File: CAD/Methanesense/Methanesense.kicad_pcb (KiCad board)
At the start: 4 copper layers, 31.4 x 21 mm, 69 parts, among them J1 Conn_01x06_Pin, J2 SM12B-GHS-TB(LF)(SN), U1 AP63201WU, U2 ADS1115IDGS, U3 ESP32-C3-WROOM-02, U4 LP5907MFX-3.0, U5 MCP4725xxx-xCH, Y1 32.768khz 3215 12.5pf

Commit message: WIP
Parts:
- removed D1, D2, D3, D4: 1N5819WS, Diode_SMD:D_SOD-323
- removed R14: 182k, Resistor_SMD:R_0402_1005Metric
- removed R15: 62k, Resistor_SMD:R_0402_1005Metric
- removed R16: 10K, Resistor_SMD:R_0402_1005Metric
- removed U1: AP63201WU, Package_TO_SOT_SMD:TSOT-23-6
- removed Y1: 32.768khz 3215 12.5pf, Crystal:Crystal_SMD_3215-2Pin_3.2x1.5mm
- removed kibuzzard-65D3616E: G***, esprelay:kibuzzard-65D3616E
- removed kibuzzard-65D36177: G***, esprelay:kibuzzard-65D36177
- removed kibuzzard-65D46022: G***, esprelay:kibuzzard-65D46022
- removed kibuzzard-65D46066: G***, esprelay:kibuzzard-65D46066
- removed kibuzzard-65D460A0: G***, esprelay:kibuzzard-65D460A0
- removed kibuzzard-65D49092: G***, kibuzzard-65D49092
- removed kibuzzard-65D7176D: G***, kibuzzard-65D7176D
- removed kibuzzard-65D71774: G***, kibuzzard-65D71774
- removed kibuzzard-65D7177B: G***, kibuzzard-65D7177B
- removed kibuzzard-65D74DE1: G***, kibuzzard-65D74DE1
- removed kibuzzard-65D74DEE: G***, kibuzzard-65D74DEE
- removed kibuzzard-65D74DFB: G***, kibuzzard-65D74DFB
- removed kibuzzard-65D8B121: G***, kibuzzard-65D8B121
- removed kibuzzard-65DC95DA: G***, kibuzzard-65DC95DA
- removed kibuzzard-65DC95E5: G***, kibuzzard-65DC95E5
- removed kibuzzard-65DC95EF: G***, kibuzzard-65DC95EF
- removed kibuzzard-65DC95F6: G***, kibuzzard-65DC95F6
- removed kibuzzard-65DC9610: G***, kibuzzard-65DC9610
- removed kibuzzard-65DC961D: G***, kibuzzard-65DC961D
- removed kibuzzard-65DCE4DE: G***, kibuzzard-65DCE4DE
- added BT1: 1042P, Battery:BatteryHolder_MPD_BH-18650-PC2, B.Cu at (64.8, 63.2)
- added C21: 47uF, Capacitor_SMD:C_0805_2012Metric, F.Cu at (44.8, 53.8)
- added C22: 47uF, Capacitor_SMD:C_0805_2012Metric, F.Cu at (63.8, 53.9)
- added C23: 4.7uF, Capacitor_SMD:C_0603_1608Metric, F.Cu at (57.2, 51.0)
- added C24: 1nF, Capacitor_SMD:C_0603_1608Metric, F.Cu at (62.4, 68.0)
- added C25: 4.7uF, Capacitor_SMD:C_0603_1608Metric, F.Cu at (51.2, 51.0)
- added C26: 15pF, Methanesense:C_0603_1608Metric, F.Cu at (54.6, 69.1)
- added C27: 15pF, Methanesense:C_0603_1608Metric, F.Cu at (54.4, 70.9)
- added C28: 1uF, Capacitor_SMD:C_0603_1608Metric, F.Cu at (68.7, 69.0)
- added C29: 56pF, Capacitor_SMD:C_0603_1608Metric, F.Cu at (62.2, 71.4)
- added C30: 56pF, Capacitor_SMD:C_0603_1608Metric, F.Cu at (60.2, 72.1)
- added C31: 1uF, Capacitor_SMD:C_0603_1608Metric, F.Cu at (66.6, 53.8)
- added C32: 0.1uF, Capacitor_SMD:C_0603_1608Metric, F.Cu at (47.6, 53.6)
- added C33: 15pF, Capacitor_SMD:C_0603_1608Metric, F.Cu at (46.3, 53.6)
- added C34: 0.1uF, Capacitor_SMD:C_0603_1608Metric, F.Cu at (62.2, 53.7)
- added C35: 15pF, Capacitor_SMD:C_0603_1608Metric, F.Cu at (60.8, 53.7)
- added C36: 0.1uF, Capacitor_SMD:C_0603_1608Metric, F.Cu at (54.4, 51.0)
- added C37: 10uF, Capacitor_SMD:C_0805_2012Metric, F.Cu at (88.6, 62.8)
- added C38: 0.1uF, Capacitor_SMD:C_0603_1608Metric, F.Cu at (139.0, 52.4)
- added C39: 1uF, Capacitor_SMD:C_0603_1608Metric, F.Cu at (137.5, 52.4)
- added D10: LED, LED_SMD:LED_0603_1608Metric, F.Cu at (80.7, 87.8)
- added D11: LED, LED_SMD:LED_0603_1608Metric, F.Cu at (80.7, 90.4)
- added D5: LED, LED_SMD:LED_0603_1608Metric, F.Cu at (95.6, 53.6)
- added D6: LED, LED_SMD:LED_0603_1608Metric, F.Cu at (98.6, 53.6)
- added D9: LED, LED_SMD:LED_0603_1608Metric, F.Cu at (80.7, 85.2)
- added F1: 0805L110WR, Resistor_SMD:R_1206_3216Metric, F.Cu at (68.8, 63.4)
- added J3: 693043020611, Methanesense:693043020611, F.Cu at (74.8, 55.5)
- added J4: Conn_Coaxial, Connector_Coaxial:U.FL_Hirose_U.FL-R-SMT-1_Vertical, F.Cu at (66.2, 72.2)
- added J6: JLINK, esprelay:SEXY_pinpogo, B.Cu at (47.0, 61.0)
- added J7: Conn_02x05_Odd_Even, Connector_PinHeader_2.54mm:PinHeader_2x05_P2.54mm_Vertical, F.Cu at (74.8, 42.8)
- added L2: 39NH, Methanesense:L_0603_1608Metric, F.Cu at (56.4, 72.0)
- added L3: 2.2uH, Inductor_SMD:L_1008_2520Metric, F.Cu at (86.2, 70.2)
- added L4: NP, Methanesense:L_0603_1608Metric, F.Cu at (49.8, 73.9)
- added L5: 7.5NH, Methanesense:L_0603_1608Metric, F.Cu at (46.0, 73.9)
- added L6: 1.6nH, Methanesense:L_0603_1608Metric, F.Cu at (44.1, 74.5)
- added L7: 39NH, Methanesense:L_0603_1608Metric, F.Cu at (51.8, 70.7)
- added L8: 68 nH, Methanesense:L_0603_1608Metric, F.Cu at (63.6, 71.5)
- added NT1: NetTie_2, esprelay:Viatie, F.Cu at (89.7, 68.0)
- added Q1: FDS6892A, Package_SO:SOIC-8_3.9x4.9mm_P1.27mm, F.Cu at (128.8, 70.1)
- added Q2: FDS6892A, Package_SO:SOIC-8_3.9x4.9mm_P1.27mm, F.Cu at (97.2, 58.2)
- added R17: 1M, Resistor_SMD:R_0603_1608Metric, F.Cu at (68.7, 67.1)
- added R18: 100R, Capacitor_SMD:C_0603_1608Metric, F.Cu at (65.9, 56.6)
- added R19: 100R, Capacitor_SMD:C_0603_1608Metric, F.Cu at (65.9, 58.1)
- added R20: 100R, Capacitor_SMD:C_0603_1608Metric, F.Cu at (65.9, 59.6)
- added R22: 120R, Capacitor_SMD:C_0603_1608Metric, F.Cu at (98.6, 52.0)
- added R23: 120R, Capacitor_SMD:C_0603_1608Metric, F.Cu at (95.6, 52.0)
- added R24: 1M, Resistor_SMD:R_0603_1608Metric, F.Cu at (98.8, 62.6)
- added R25: 1M, Resistor_SMD:R_0603_1608Metric, F.Cu at (95.8, 62.6)
- added R26: 1k, Capacitor_SMD:C_0603_1608Metric, F.Cu at (168.8, 96.2)
- added S1: TGS8410, Methanesense:TGS8410, B.Cu at (145.9, 70.8)
- added SW1: KMR223GLFG, Button_Switch_SMD:SW_Push_1P1T_NO_CK_KMR2, F.Cu at (171.1, 82.4)
- added SW2: JS202011JCQN, Button_Switch_SMD:SW_DIP_SPSTx01_Slide_6.7x4.1mm_W6.73mm_P2.54mm_LowProfile_JPin, F.Cu at (165.9, 92.7)
- added SW3: KMR223GLFG, Button_Switch_SMD:SW_Push_1P1T_NO_CK_KMR2, F.Cu at (77.5, 81.6)
- added TH1: 10k NTC, Resistor_SMD:R_0603_1608Metric, F.Cu at (84.0, 90.9)
- added U6: BME680, Package_LGA:Bosch_LGA-8_3x3mm_P0.8mm_ClockwisePinNumbering, F.Cu at (148.4, 52.0)
- added U7: FT230XQ, Package_DFN_QFN:QFN-16-1EP_4x4mm_P0.65mm_EP2.1x2.1mm, F.Cu at (127.4, 56.8)
- added U8: USBLC6-4SC6, Package_TO_SOT_SMD:SOT-23-6, F.Cu at (62.1, 58.3)
- added U9: TPS22917DBV, Package_TO_SOT_SMD:SOT-23-6, F.Cu at (65.2, 68.0)
- C1: value 20pf -> 1.7pF; footprint Capacitor_SMD:C_0402_1005Metric -> Methanesense:C_0603_1608Metric
- C10: value 0.1uF -> 10uF; footprint Capacitor_SMD:C_0402_1005Metric -> Capacitor_SMD:C_0805_2012Metric
- C11, C8: value 22uf -> 1uF; footprint Capacitor_SMD:C_0402_1005Metric -> Capacitor_SMD:C_0603_1608Metric
- C12: value 22uf -> 10uF; footprint Capacitor_SMD:C_0402_1005Metric -> Capacitor_SMD:C_0805_2012Metric
- C13, C14, C15, C16, C20: footprint Capacitor_SMD:C_0402_1005Metric -> Capacitor_SMD:C_0603_1608Metric
- C17, C18, C9: value 0.1uF -> 1uF; footprint Capacitor_SMD:C_0402_1005Metric -> Capacitor_SMD:C_0603_1608Metric
- C19: value 1uF -> 0.1uF; footprint Capacitor_SMD:C_0402_1005Metric -> Capacitor_SMD:C_0603_1608Metric
- C2: value 0.1uF -> 1.7pF; footprint Capacitor_SMD:C_0402_1005Metric -> Methanesense:C_0603_1608Metric
- C3, C6: value 0.1uF -> 47pF; footprint Capacitor_SMD:C_0402_1005Metric -> Capacitor_SMD:C_0603_1608Metric
- C4: value 20pf -> 8.5pF; footprint Capacitor_SMD:C_0402_1005Metric -> Methanesense:C_0603_1608Metric
- C5: value 10uF -> 15pF; footprint Capacitor_SMD:C_0805_2012Metric -> Methanesense:C_0603_1608Metric
- C7: value 10uF -> 1uF; footprint Capacitor_SMD:C_0805_2012Metric -> Capacitor_SMD:C_0603_1608Metric
- J1: value Conn_01x06_Pin -> USB_C_Receptacle_USB2.0_14P; footprint TestPoint:TestPoint_Pad_1.0x1.0mm_6pad -> Methanesense:USB_C_Receptacle_HCTL_HC-TYPE-C-16P-01A; moved to F.Cu
- J2: value SM12B-GHS-TB(LF)(SN) -> Conn_Coaxial; footprint Connector_JST:JST_GH_SM12B-GHS-TB_1x12-1MP_P1.25mm_Horizontal -> Connector_Coaxial:U.FL_Hirose_U.FL-R-SMT-1_Vertical
- L1: value 6.8uH -> 2.3nH; footprint Inductor_SMD:L_1008_2520Metric -> Methanesense:L_0603_1608Metric
- R1: value 10K -> 68k; footprint Resistor_SMD:R_0402_1005Metric -> Resistor_SMD:R_0603_1608Metric
- R10, R11: value 499R -> 1M; footprint Resistor_SMD:R_0402_1005Metric -> Resistor_SMD:R_0603_1608Metric
- R12: value 10K -> 10k; footprint Resistor_SMD:R_0402_1005Metric -> Resistor_SMD:R_0603_1608Metric
- R13: value 100R -> 10k; footprint Resistor_SMD:R_0402_1005Metric -> Resistor_SMD:R_0603_1608Metric
- R2, R3, R4, R5: value 10K -> 499R
- R6: footprint Resistor_SMD:R_0402_1005Metric -> Resistor_SMD:R_0603_1608Metric
- R7: value 309k -> 499R
- R9: value 499R -> <2k; footprint Resistor_SMD:R_0402_1005Metric -> Resistor_SMD:R_0603_1608Metric
- U3: value ESP32-C3-WROOM-02 -> nPM1300-QEXX; footprint PCM_Espressif:ESP32-C3-WROOM-02 -> Package_DFN_QFN:QFN-32-1EP_5x5mm_P0.5mm_EP3.6x3.6mm; moved to F.Cu
- U4: value LP5907MFX-3.0 -> AP7331-20WG-7
- U5: value MCP4725xxx-xCH -> nRF9160-SICA; footprint Package_TO_SOT_SMD:SOT-23-6 -> PCM_nordic-lib-kicad-nrf9:LGA_9160_16.0x10.5mm
- moved J2 81.1 mm to (48.4, 71.3), turned to 180 degrees
- moved U5 69.0 mm to (54.5, 60.0)
- moved C2 68.7 mm to (51.0, 73.9), turned to 90 degrees
- moved C5 67.7 mm to (53.5, 70.9), turned to -135 degrees
- moved L1 64.3 mm to (52.9, 74.5), turned to 180 degrees
- moved C4 63.2 mm to (47.8, 74.5), turned to 180 degrees
- moved C7 54.3 mm to (136.3, 35.9), turned to 0 degrees
- moved C1 54.1 mm to (55.3, 74.5), turned to 180 degrees
- moved U4 53.8 mm to (136.4, 33.3), turned to 180 degrees
- moved C9 49.9 mm to (136.4, 30.9), turned to 0 degrees
- moved C6 47.2 mm to (132.1, 39.6), turned to 0 degrees
- moved C8 44.5 mm to (139.2, 33.3), turned to 90 degrees
- moved C3 44.2 mm to (132.1, 37.1), turned to 0 degrees
- moved R12 38.7 mm to (134.5, 52.4), turned to 90 degrees
- moved R13 38.4 mm to (136.0, 52.4), turned to 90 degrees
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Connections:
- C1 pad 1: GND -> Net-(C1-Pad1)
- C1 pad 2: Net-(U3-GPIO0/ADC1_CH0/XTAL_32K_P) -> Net-(C1-Pad2)
- C10 pad 1: +3.3V -> +2V0
- C10 pad 2: GND -> PVSS1
- C11 pad 1: +3.3V -> +5V
- C12 pad 1: +3.3V -> VSYS
- C13 pad 1: +3V0 -> GND
- C13 pad 2: GND -> Net-(U2-AIN0)
- C14 pad 1: +3.3V -> GND
- C14 pad 2: GND -> Net-(U2-AIN1)
- C15 pad 2: Net-(U2-AIN0) -> Net-(U2-AIN2)
- C16 pad 2: Net-(U2-AIN1) -> Net-(U2-AIN3)
- C17 pad 1: GND -> Net-(U2-AIN0)
- C17 pad 2: Net-(U2-AIN2) -> Net-(U2-AIN1)
- C18 pad 1: GND -> Net-(U2-AIN2)
- C19 pad 1: Net-(U2-AIN0) -> +2V0
- C19 pad 2: Net-(U2-AIN1) -> GND
- C2 pad 1: /SW -> Net-(C2-Pad1)
- C2 pad 2: Net-(U1-BST) -> GND
- C20 pad 1: Net-(U2-AIN2) -> +2V0
- C20 pad 2: Net-(U2-AIN3) -> GND
- C3 pad 1: +3.3V -> GND
- C3 pad 2: GND -> Net-(U7-USBDM)
- C4 pad 1: Net-(U3-GPIO1/ADC1_CH1/XTAL_32K_N) -> Net-(C2-Pad1)
- C4 pad 2: GND -> Net-(C4-Pad2)
- C5 pad 1: /VIN_P -> /nrf9160/ANT
- C5 pad 2: GND -> Net-(J2-In)
- C6 pad 1: +3V0 -> GND
- C6 pad 2: GND -> Net-(U7-USBDP)
- C7 pad 1: +3V0 -> Net-(U4-OUT)
- C8 pad 1: +3.3V -> +5VL
- C9 pad 1: +3.3V -> Net-(U4-BP)
- C9 pad 2: /FB -> GND
- J2 pad 1: +3.3V -> Net-(J2-In)
- J2 pad 2: ONEWIRE_OUT -> GND
- L1 pad 1: /SW -> Net-(C1-Pad2)
- L1 pad 2: +3.3V -> Net-(C2-Pad1)
- R1 pad 1: +3.3V -> Net-(U3-VSET1)
- R1 pad 2: RST -> GND
- R10 pad 1: Net-(U2-AIN2) -> GND
- R10 pad 2: AIN2 -> /Sensor
- R11 pad 1: Net-(U2-AIN3) -> GND
- R11 pad 2: AIN3 -> /Heater
- R12 pad 1: ADC_DRDY -> /nrf9160/SDA
- R12 pad 2: +3.3V -> +2V0
- R13 pad 1: ONEWIRE_OUT -> /nrf9160/SCL
- R13 pad 2: ONEWIRE -> +2V0
- R2 pad 1: +3.3V -> Net-(U2-AIN0)
- R2 pad 2: BOOT -> AIN0
- R3 pad 1: ADC -> Net-(U2-AIN1)
- R3 pad 2: GND -> AIN1
- R4 pad 1: Net-(U3-GPIO8) -> Net-(U2-AIN2)
- R4 pad 2: +3.3V -> AIN2
- R5 pad 1: SDA -> Net-(U2-AIN3)
- R5 pad 2: +3.3V -> AIN3
- R6 pad 1: +3.3V -> /ADC_DRDY
- R6 pad 2: ONEWIRE -> +2V0
- R7 pad 1: /VIN_P -> AIN0
- R7 pad 2: ADC -> AIN0
- R8 pad 1: Net-(U2-AIN0) -> AIN1
- R8 pad 2: AIN0 -> AIN1
- R9 pad 1: Net-(U2-AIN1) -> AIN1
- R9 pad 2: AIN1 -> AIN0
- U2 pad 10: SCL -> /SCL
- U2 pad 2: ADC_DRDY -> /ADC_DRDY
- U2 pad 8: +3V0 -> +2V0
- U2 pad 9: SDA -> /SDA
- U3 pad 1: +3.3V -> +2V0
- U3 pad 10: ADC_DRDY -> unconnected-(U3-GPIO3-Pad10)
- U3 pad 11: RX -> unconnected-(U3-GPIO4-Pad11)
- U3 pad 12: TX -> +2V0
- U3 pad 13: unconnected-(U3-GPIO18/USB_D--Pad13) -> /SDA
- U3 pad 14: SCL -> /SCL
- U3 pad 15: ONEWIRE -> Net-(U3-SHPHLD)
- U3 pad 16: SDA -> GND
- U3 pad 17: Net-(U3-GPIO1/ADC1_CH1/XTAL_32K_N) -> Net-(U3-VSET1)
- U3 pad 18: Net-(U3-GPIO0/ADC1_CH0/XTAL_32K_P) -> Net-(U3-NTC)
- U3 pad 19: GND -> +BATT
- U3 pad 2: RST -> PVSS1
- U3 pad 3: ADC -> /POWER/SW1
- U3 pad 4: unconnected-(U3-GPIO5/ADC2_CH0-Pad4) -> VSYS
- U3 pad 6: unconnected-(U3-GPIO7-Pad6) -> GND
- U3 pad 7: Net-(U3-GPIO8) -> unconnected-(U3-GPIO0-Pad7)
- U3 pad 8: BOOT -> unconnected-(U3-GPIO1-Pad8)
- U3 pad 9: GND -> unconnected-(U3-GPIO2-Pad9)
- U4 pad 1: +3.3V -> +5VL
- U4 pad 3: ENBL_PSUP -> +5VL
- U4 pad 4: unconnected-(U4-NC-Pad4) -> Net-(U4-BP)
- U4 pad 5: +3V0 -> Net-(U4-OUT)
- U5 pad 1: AOUT0 -> GND
- U5 pad 2: GND -> /nrf9160/P0.05
- U5 pad 3: +3.3V -> /nrf9160/P0.06
- U5 pad 4: SDA -> /nrf9160/P0.07
- U5 pad 5: SCL -> GND
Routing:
- net +3.3V: track 105.2 -> 0.00 mm, vias 10 -> 0
- net GND: track 42.8 -> 128.4 mm, vias 72 -> 65
- net +1V8SIM: track 0.00 -> 38.6 mm, vias 0 -> 2
- net +3V0: track 32.5 -> 0.00 mm, vias 2 -> 0
- net /nrf9160/SIM_CLK: track 0.00 -> 28.7 mm, vias 0 -> 2
- net /nrf9160/SIM_RST: track 0.00 -> 28.5 mm, vias 0 -> 2
- net /nrf9160/SIM_IO: track 0.00 -> 27.5 mm, vias 0 -> 2
- net SDA: track 27.2 -> 0.00 mm, vias 2 -> 0
- net SCL: track 25.6 -> 0.00 mm, vias 2 -> 0
- net RST: track 21.3 -> 0.00 mm, vias 2 -> 0
- net ONEWIRE: track 19.0 -> 0.00 mm, vias 1 -> 0
- net ADC_DRDY: track 17.9 -> 0.00 mm, vias 1 -> 0
- net BOOT: track 17.7 -> 0.00 mm, vias 1 -> 0
- net /nrf9160/COEX0: track 0.00 -> 16.2 mm
- net /VIN_P: track 16.2 -> 0.00 mm, vias 2 -> 0
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- removed copper zone on B.Cu, net +3.3V
- removed copper zone on F.Cu, net +3.3V
- removed copper zone on In1.Cu, net +3.3V
- removed copper zone on F.Cu, net +VDC
- removed copper zone on F.Cu, net /VIN_P
- removed copper zone on B.Cu, net GND
- removed copper zone on F.Cu, net GND
- removed copper zone on In1.Cu, net GND
- removed copper zone on In2.Cu, net GND
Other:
- board size 31.4 x 21 mm -> 120 x 25 mm
- board text removed: "1"
- board text removed: "2"
- board text removed: "3"
- board text removed: "4"

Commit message: WIP
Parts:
- removed NT1: NetTie_2, esprelay:Viatie
- BT1: moved to F.Cu
- moved TH1 31.2 mm to (70.9, 62.6)
- moved R1 27.0 mm to (73.6, 63.0), turned to 90 degrees
- moved SW3 19.0 mm to (77.2, 62.6), turned to 180 degrees
- moved D11 18.2 mm to (77.5, 72.5), turned to -90 degrees
- moved D10 16.0 mm to (76.0, 72.5), turned to -90 degrees
- moved C11 15.6 mm to (72.5, 68.5), turned to 180 degrees
- moved D9 14.1 mm to (74.5, 72.5), turned to -90 degrees
- moved C10 6.90 mm to (81.7, 70.2)
- moved C37 5.30 mm to (84.1, 65.6), turned to 90 degrees
- moved C12 4.45 mm to (82.1, 65.6), turned to 90 degrees
- moved U3 4.16 mm to (77.5, 67.5)
- moved C21 3.15 mm to (46.6, 51.2), turned to 180 degrees
- moved L3 2.06 mm to (84.2, 69.7)
- moved C29 1.38 mm to (61.4, 70.3), turned to 180 degrees
- moved F1 0.20 mm to (69.0, 63.4)
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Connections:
- C10 pad 2: PVSS1 -> GND
- U3 pad 2: PVSS1 -> GND
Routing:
- net +5VL: track 0.00 -> 50.7 mm, vias 0 -> 3
- net GND: track 128.4 -> 165.4 mm, vias 65 -> 79
- net +5V: track 11.3 -> 36.8 mm, vias 0 -> 3
- net +2V0: track 2.88 -> 16.0 mm
- net VSYS: track 0.00 -> 13.0 mm, vias 0 -> 4
- net +BATT: track 0.00 -> 6.83 mm
- net Net-(BT1-+): track 0.00 -> 4.66 mm
- net /POWER/SW1: track 0.00 -> 4.41 mm
- net /POWER/CC1: track 0.00 -> 2.78 mm, vias 0 -> 1
- net Net-(D9-K): track 0.00 -> 2.28 mm
- net /nrf9160/SIM_IO: track 27.5 -> 29.8 mm
- net Net-(D11-K): track 0.00 -> 2.07 mm
- net Net-(U3-SHPHLD): track 0.00 -> 2.00 mm
- net Net-(D10-K): track 0.00 -> 1.87 mm
- net Net-(U9-VOUT): track 2.09 -> 3.54 mm
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- added copper zone on F.Cu, net +2V0
- added copper zone on F.Cu, net +5V
- added copper zone on F.Cu, net /POWER/SW1
- added copper zone on F.Cu, net GND
- added copper zone on F.Cu, net VSYS

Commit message: Allmost there
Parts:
- removed C15, C16: 0.1uF, Capacitor_SMD:C_0603_1608Metric
- removed C18: 1uF, Capacitor_SMD:C_0603_1608Metric
- removed J7: Conn_02x05_Odd_Even, Connector_PinHeader_2.54mm:PinHeader_2x05_P2.54mm_Vertical
- removed R12, R13: 10k, Resistor_SMD:R_0603_1608Metric
- removed R6: 10K, Resistor_SMD:R_0603_1608Metric
- added AE1: NN02-220, Methanesense:XCVR_NN02-220, F.Cu at (37.0, 63.0)
- BT1: value 1042P -> BH-18650-PC2; footprint Battery:BatteryHolder_MPD_BH-18650-PC2 -> Methanesense:BatteryHolder_MPD_BH-18650-PC2; moved to B.Cu
- R2, R3: footprint Resistor_SMD:R_0402_1005Metric -> Resistor_SMD:R_0603_1608Metric
- R4, R5, R7, R8: value 499R -> 0R; footprint Resistor_SMD:R_0402_1005Metric -> Resistor_SMD:R_0603_1608Metric
- moved SW1 84.4 mm to (89.0, 62.6)
- moved R26 78.8 mm to (103.4, 52.2), turned to 180 degrees
- moved SW2 72.3 mm to (102.6, 57.8), turned to 90 degrees
- moved R4 62.1 mm to (78.8, 72.0), turned to 90 degrees
- moved R5 30.4 mm to (124.0, 58.2)
- moved C9 28.4 mm to (126.4, 57.4), turned to 90 degrees
- moved C19 27.8 mm to (124.0, 68.6), turned to 90 degrees
- moved C20 27.2 mm to (124.0, 71.8), turned to -90 degrees
- moved U4 25.3 mm to (128.8, 57.4), turned to -90 degrees
- moved C8 23.8 mm to (128.7, 54.6), turned to 180 degrees
- moved C7 22.2 mm to (131.3, 57.5), turned to 90 degrees
- moved R8 21.0 mm to (131.9, 68.7), turned to 90 degrees
- moved C6 20.6 mm to (139.2, 59.0), turned to 90 degrees
- moved C3 20.4 mm to (139.2, 56.2), turned to -90 degrees
- moved R11 18.7 mm to (114.9, 69.0), turned to -90 degrees
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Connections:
- net Net-(U7-USBDM) renamed /POWER/USBDN
- net Net-(U7-USBDP) renamed /POWER/USBDP
- C13 pad 2: Net-(U2-AIN0) -> /GAS_SENSOR/AIN0_
- C14 pad 2: Net-(U2-AIN1) -> /GAS_SENSOR/AIN1_
- C17 pad 1: Net-(U2-AIN0) -> /GAS_SENSOR/AIN0_
- C17 pad 2: Net-(U2-AIN1) -> /GAS_SENSOR/AIN1_
- C19 pad 1: +2V0 -> +2V0SW
- C20 pad 1: +2V0 -> +2V0SW
- C38 pad 1: +2V0 -> +2V0SW
- C39 pad 1: +2V0 -> +2V0SW
- C7 pad 1: Net-(U4-OUT) -> /POWER/VCCIOUSB
- Q1 pad 5: AIN1 -> Net-(S1-Rh-)
- Q1 pad 6: AIN1 -> Net-(S1-Rh-)
- Q1 pad 7: Net-(S1-Rh-) -> AIN0
- Q1 pad 8: Net-(S1-Rh-) -> AIN0
- R2 pad 1: Net-(U2-AIN0) -> /GAS_SENSOR/AIN0_
- R3 pad 1: Net-(U2-AIN1) -> /GAS_SENSOR/AIN1_
- R4 pad 1: Net-(U2-AIN2) -> +2V0
- R4 pad 2: AIN2 -> +2V0SW
- R5 pad 1: Net-(U2-AIN3) -> /POWER/USB_DET
- R5 pad 2: AIN3 -> /POWER/VCCIOUSB
- R7 pad 1: AIN0 -> /GAS_SENSOR/NRF_AIN0
- R7 pad 2: AIN0 -> /GAS_SENSOR/AIN0_
- R8 pad 1: AIN1 -> /GAS_SENSOR/AIN1_
- R8 pad 2: AIN1 -> /GAS_SENSOR/NRF_AIN1
- R9 pad 1: AIN1 -> AIN0
- R9 pad 2: AIN0 -> AIN1
- S1 pad 2: AIN0 -> AIN1
- S1 pad 3: +2V0 -> +2V0SW
- S1 pad 4: +2V0 -> +2V0SW
- U2 pad 4: Net-(U2-AIN0) -> /GAS_SENSOR/AIN0_
- U2 pad 5: Net-(U2-AIN1) -> /GAS_SENSOR/AIN1_
- U2 pad 6: Net-(U2-AIN2) -> AIN2
- U2 pad 7: Net-(U2-AIN3) -> AIN3
- U2 pad 8: +2V0 -> +2V0SW
- U3 pad 28: +2V0 -> unconnected-(U3-LSIN1/VINLDO1-Pad28)
- U3 pad 31: GND -> +2V0SW
- U4 pad 5: Net-(U4-OUT) -> /POWER/VCCIOUSB
- U6 pad 2: +2V0 -> +2V0SW
- U6 pad 6: +2V0 -> +2V0SW
- U6 pad 8: +2V0 -> +2V0SW
- U7 pad 1: Net-(U4-OUT) -> /POWER/VCCIOUSB
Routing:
- net +2V0: track 16.0 -> 161.8 mm, vias 1 -> 7
- net +2V0SW: track 0.00 -> 132.0 mm, vias 0 -> 6
- net /SDA: track 0.00 -> 123.4 mm, vias 0 -> 3
- net /SCL: track 0.00 -> 120.1 mm, vias 0 -> 3
- net /~{CTS}: track 0.00 -> 100.9 mm, vias 0 -> 3
- net /GAS_SENSOR/NRF_AIN0: track 0.00 -> 94.3 mm, vias 0 -> 1
- net /RXD: track 0.00 -> 90.9 mm, vias 0 -> 1
- net /POWER/CC2: track 1.41 -> 89.7 mm, vias 1 -> 2
- net /POWER/CC1: track 2.78 -> 90.6 mm, vias 1 -> 2
- net /GAS_SENSOR/NRF_AIN1: track 0.00 -> 87.4 mm, vias 0 -> 1
- net /ADC_DRDY: track 0.00 -> 85.5 mm, vias 0 -> 1
- net /~{RTS}: track 0.00 -> 85.4 mm, vias 0 -> 1
- net /TXD: track 0.00 -> 84.9 mm, vias 0 -> 1
- net /Sensor: track 0.00 -> 67.4 mm, vias 0 -> 1
- net +5VL: track 50.7 -> 118.1 mm, vias 3 -> 7
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- added copper zone on B.Cu, net +2V0SW
- added copper zone on F.Cu, net +2V0SW
- added copper zone on B.Cu, net +5VL
- added copper zone on B.Cu, net GND
- added copper zone on In1.Cu, net GND
- added copper zone on In2.Cu, net GND
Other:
- board size 120 x 25 mm -> 120.3 x 25.6 mm
- board text added: "SIMCARD KEEPOUT"

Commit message: WIP
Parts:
- added J5: Conn_01x10_Pin, Connector_PinHeader_2.54mm:PinHeader_1x10_P2.54mm_Vertical, F.Cu at (106.8, 51.6)
- C26, C27, C5: footprint Methanesense:C_0603_1608Metric -> Methanesense:C_0402_1005Metric_Sqr
- C29, C30: footprint Capacitor_SMD:C_0603_1608Metric -> Methanesense:C_0402_1005Metric_Sqr
- L2, L7, L8: footprint Methanesense:L_0603_1608Metric -> Methanesense:C_0402_1005Metric_Sqr
- moved J4 2.92 mm to (62.8, 72.2)
- moved L8 2.84 mm to (60.3, 71.8)
- moved C30 1.55 mm to (58.8, 71.5), turned to -45 degrees
- moved L2 0.88 mm to (55.7, 71.5)
- moved C29 0.72 mm to (60.3, 69.9), turned to 90 degrees
- moved L7 0.53 mm to (52.3, 70.8)
- moved C5 0.15 mm to (53.7, 70.9)
- moved C26 0.13 mm to (54.5, 69.1)
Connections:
- net /nrf9160/COEX0 renamed COEX0
- net /nrf9160/P0.05 renamed P0.05
- net /nrf9160/P0.06 renamed P0.06
- net /nrf9160/P0.07 renamed P0.07
- net /nrf9160/P0.08 renamed P0.08
- net /nrf9160/SIM_CLK renamed SIM_CLK
- net /nrf9160/SIM_IO renamed SIM_IO
- net /nrf9160/SIM_RST renamed SIM_RST
- net /nrf9160/SWDCLK renamed SWDCLK
- net /nrf9160/SWDIO renamed SWDIO
- net /nrf9160/SWO renamed SWO
- net /nrf9160/~{RESET} renamed ~{RESET}
- Q1 pad 2: /Heater -> P0.29
- Q1 pad 4: /Sensor -> P0.31
- R10 pad 2: /Sensor -> P0.31
- R11 pad 2: /Heater -> P0.29
- R5 pad 1: /POWER/USB_DET -> P0.04
- R7 pad 1: /GAS_SENSOR/NRF_AIN0 -> P0.19/AIN6
- R8 pad 2: /GAS_SENSOR/NRF_AIN1 -> P0.18/AIN5
- U2 pad 10: /SCL -> P0.27
- U2 pad 2: /ADC_DRDY -> P0.28
- U2 pad 9: /SDA -> P0.26
- U3 pad 13: /SDA -> P0.26
- U3 pad 14: /SCL -> P0.27
- U5 pad 100: unconnected-(U5-P0.04-Pad100) -> P0.04
- U5 pad 16: unconnected-(U5-P0.09-Pad16) -> P0.09
- U5 pad 18: unconnected-(U5-P0.10-Pad18) -> P0.10
- U5 pad 19: unconnected-(U5-P0.11-Pad19) -> P0.11
- U5 pad 20: unconnected-(U5-P0.12-Pad20) -> P0.12
- U5 pad 23: unconnected-(U5-P0.13/AIN0-Pad23) -> P0.13/AIN0
- U5 pad 24: unconnected-(U5-P0.14/AIN1-Pad24) -> P0.14/AIN1
- U5 pad 25: unconnected-(U5-P0.15/AIN2-Pad25) -> P0.15/AIN2
- U5 pad 26: unconnected-(U5-P0.16/AIN3-Pad26) -> P0.16/AIN3
- U5 pad 28: unconnected-(U5-P0.17/AIN4-Pad28) -> P0.17/AIN4
- U5 pad 29: unconnected-(U5-P0.18/AIN5-Pad29) -> P0.18/AIN5
- U5 pad 30: unconnected-(U5-P0.19/AIN6-Pad30) -> P0.19/AIN6
- U5 pad 35: unconnected-(U5-P0.20/AIN7-Pad35) -> P0.20/AIN7
- U5 pad 83: unconnected-(U5-P0.26-Pad83) -> P0.26
- U5 pad 84: unconnected-(U5-P0.27-Pad84) -> P0.27
- U5 pad 86: unconnected-(U5-P0.28-Pad86) -> P0.28
- U5 pad 87: unconnected-(U5-P0.29-Pad87) -> P0.29
- U5 pad 88: unconnected-(U5-P0.30-Pad88) -> P0.30
- U5 pad 89: /nrf9160/P0.31 -> P0.31
- U5 pad 96: unconnected-(U5-P0.01-Pad96) -> P0.01
- U5 pad 97: unconnected-(U5-P0.02-Pad97) -> P0.02
- U5 pad 99: unconnected-(U5-P0.03-Pad99) -> P0.03
- U6 pad 3: /SDA -> P0.26
- U6 pad 4: /SCL -> P0.27
- U7 pad 15: /TXD -> P0.11
- U7 pad 16: /~{RTS} -> P0.14/AIN1
- U7 pad 2: /RXD -> P0.15/AIN2
- U7 pad 4: /~{CTS} -> P0.16/AIN3
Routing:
- net /SDA: track 123.4 -> 0.00 mm, vias 3 -> 0
- net P0.27: track 0.00 -> 122.4 mm, vias 0 -> 4
- net P0.26: track 0.00 -> 121.1 mm, vias 0 -> 4
- net /SCL: track 120.1 -> 0.00 mm, vias 3 -> 0
- net P0.16/AIN3: track 0.00 -> 101.8 mm, vias 0 -> 4
- net /~{CTS}: track 100.9 -> 0.00 mm, vias 3 -> 0
- net P0.19/AIN6: track 0.00 -> 95.4 mm, vias 0 -> 2
- net /GAS_SENSOR/NRF_AIN0: track 94.3 -> 0.00 mm, vias 1 -> 0
- net P0.15/AIN2: track 0.00 -> 92.1 mm, vias 0 -> 2
- net /RXD: track 90.9 -> 0.00 mm, vias 1 -> 0
- net P0.18/AIN5: track 0.00 -> 88.8 mm, vias 0 -> 2
- net /GAS_SENSOR/NRF_AIN1: track 87.4 -> 0.00 mm, vias 1 -> 0
- net P0.28: track 0.00 -> 86.5 mm, vias 0 -> 2
- net P0.14/AIN1: track 0.00 -> 86.4 mm, vias 0 -> 2
- net P0.11: track 0.00 -> 86.0 mm, vias 0 -> 2
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- added copper zone on In2.Cu, net +2V0
- added copper zone on In2.Cu, net +5V
- added copper zone on F.Cu, net +5VL
- added copper zone on B.Cu, net VSYS
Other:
- outline, holes or cut-outs redrawn
- board text added: "1"
- board text added: "2"
- board text added: "3"
- board text added: "4"
- board text added: "MINA-MethaneSense Rev 2.0"

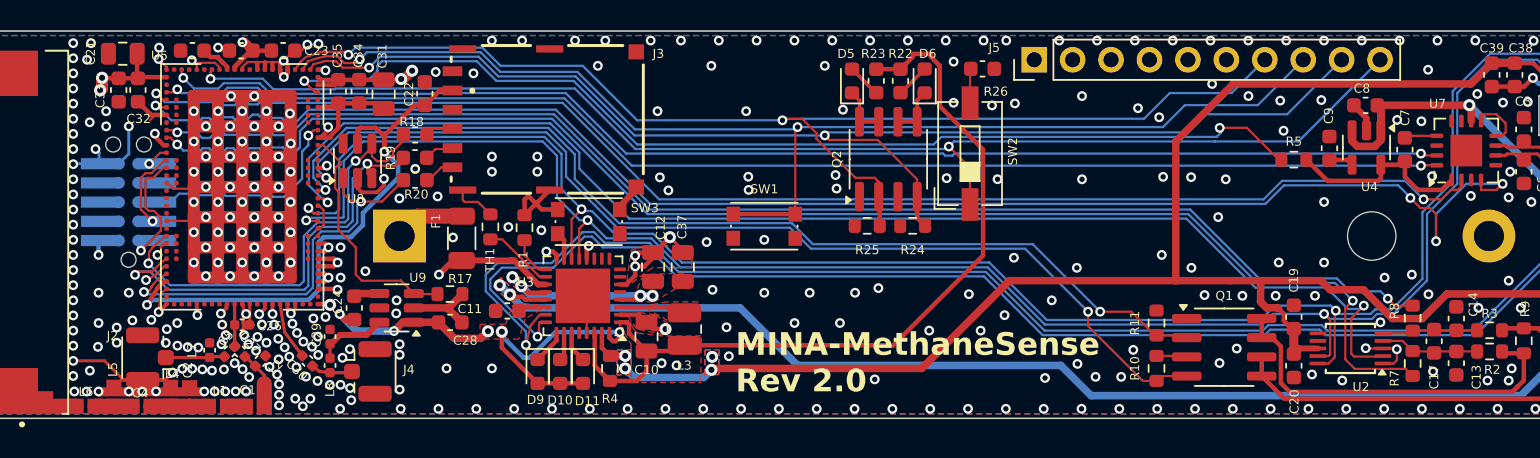
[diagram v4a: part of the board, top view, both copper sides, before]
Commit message: NRF footprint change
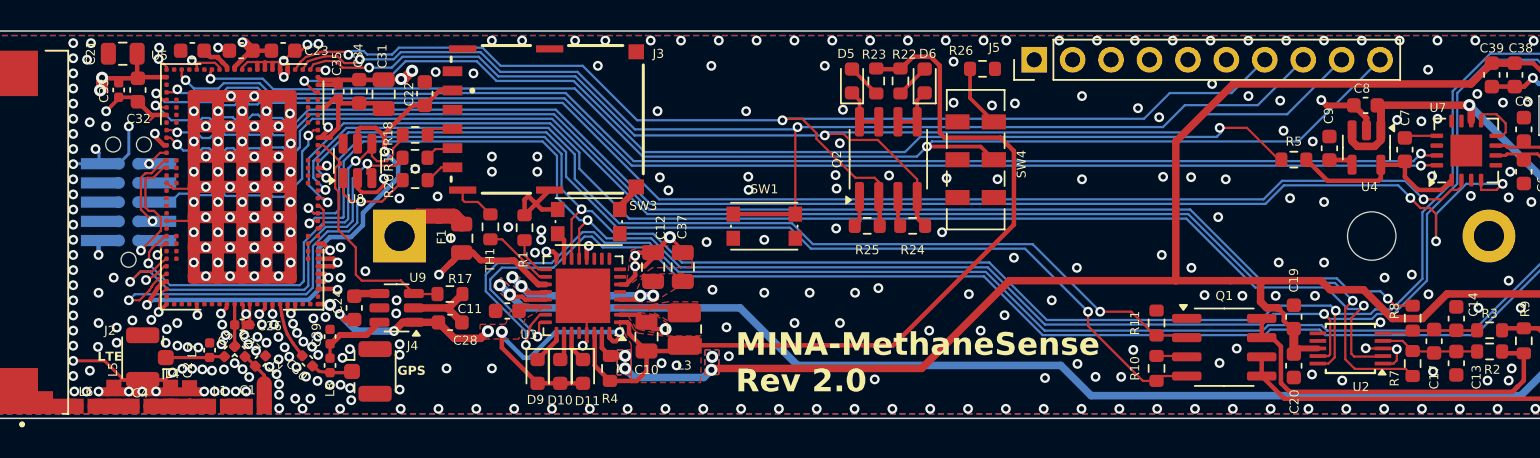
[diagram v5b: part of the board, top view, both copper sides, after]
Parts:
- removed SW2: JS202011JCQN, Button_Switch_SMD:SW_DIP_SPSTx01_Slide_6.7x4.1mm_W6.73mm_P2.54mm_LowProfile_JPin
- added SW4: JS202011JCQN, Button_Switch_SMD:SW_DPDT_CK_JS202011JCQN, F.Cu at (103.0, 58.2)
- C33, C35: footprint Capacitor_SMD:C_0603_1608Metric -> Methanesense:C_0402_1005Metric_Sqr
- F1: footprint Resistor_SMD:R_1206_3216Metric -> Fuse:Fuse_0805_2012Metric
- J2, J4: value Conn_Coaxial -> HIROSE ELECTRIC U.FL-R-SMT-1; footprint Connector_Coaxial:U.FL_Hirose_U.FL-R-SMT-1_Vertical -> Methanesense:U.FL_Hirose_U.FL-R-SMT-1_Vertical
- Q1, Q2: value FDS6892A -> FDS6898A
- R18, R19, R20, R26: footprint Capacitor_SMD:C_0603_1608Metric -> Resistor_SMD:R_0603_1608Metric
- R2, R3: value 499R -> 470R
- R22, R23: value 120R -> 100R; footprint Capacitor_SMD:C_0603_1608Metric -> Resistor_SMD:R_0603_1608Metric
- SW1, SW3: value KMR223GLFG -> KMR223NGLFG; footprint Button_Switch_SMD:SW_Push_1P1T_NO_CK_KMR2 -> Methanesense:SW_Push_1P1T_NO_CK_KMR2
- U3: footprint Package_DFN_QFN:QFN-32-1EP_5x5mm_P0.5mm_EP3.6x3.6mm -> Methanesense:QFN-32-1EP_5x5mm_P0.5mm_EP3.6x3.6mm
- U7: footprint Package_DFN_QFN:QFN-16-1EP_4x4mm_P0.65mm_EP2.1x2.1mm -> Methanesense:QFN-16-1EP_4x4mm_P0.65mm_EP2.1x2.1mm
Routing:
- net GND: track 255.6 -> 266.1 mm, vias 393 -> 403
- net +2V0: track 166.4 -> 170.3 mm
- net SIM_IO: track 27.3 -> 29.4 mm
- net Net-(SW4A-A): track 2.26 -> 4.16 mm
- net P0.08: track 86.8 -> 87.6 mm
- net SIM_CLK: track 29.1 -> 29.9 mm
- net +BATT: track 68.0 -> 68.7 mm
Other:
- board text added: "GPS"
- board text added: "LTE"
